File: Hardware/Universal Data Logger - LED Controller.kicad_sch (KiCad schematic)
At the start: 20 parts

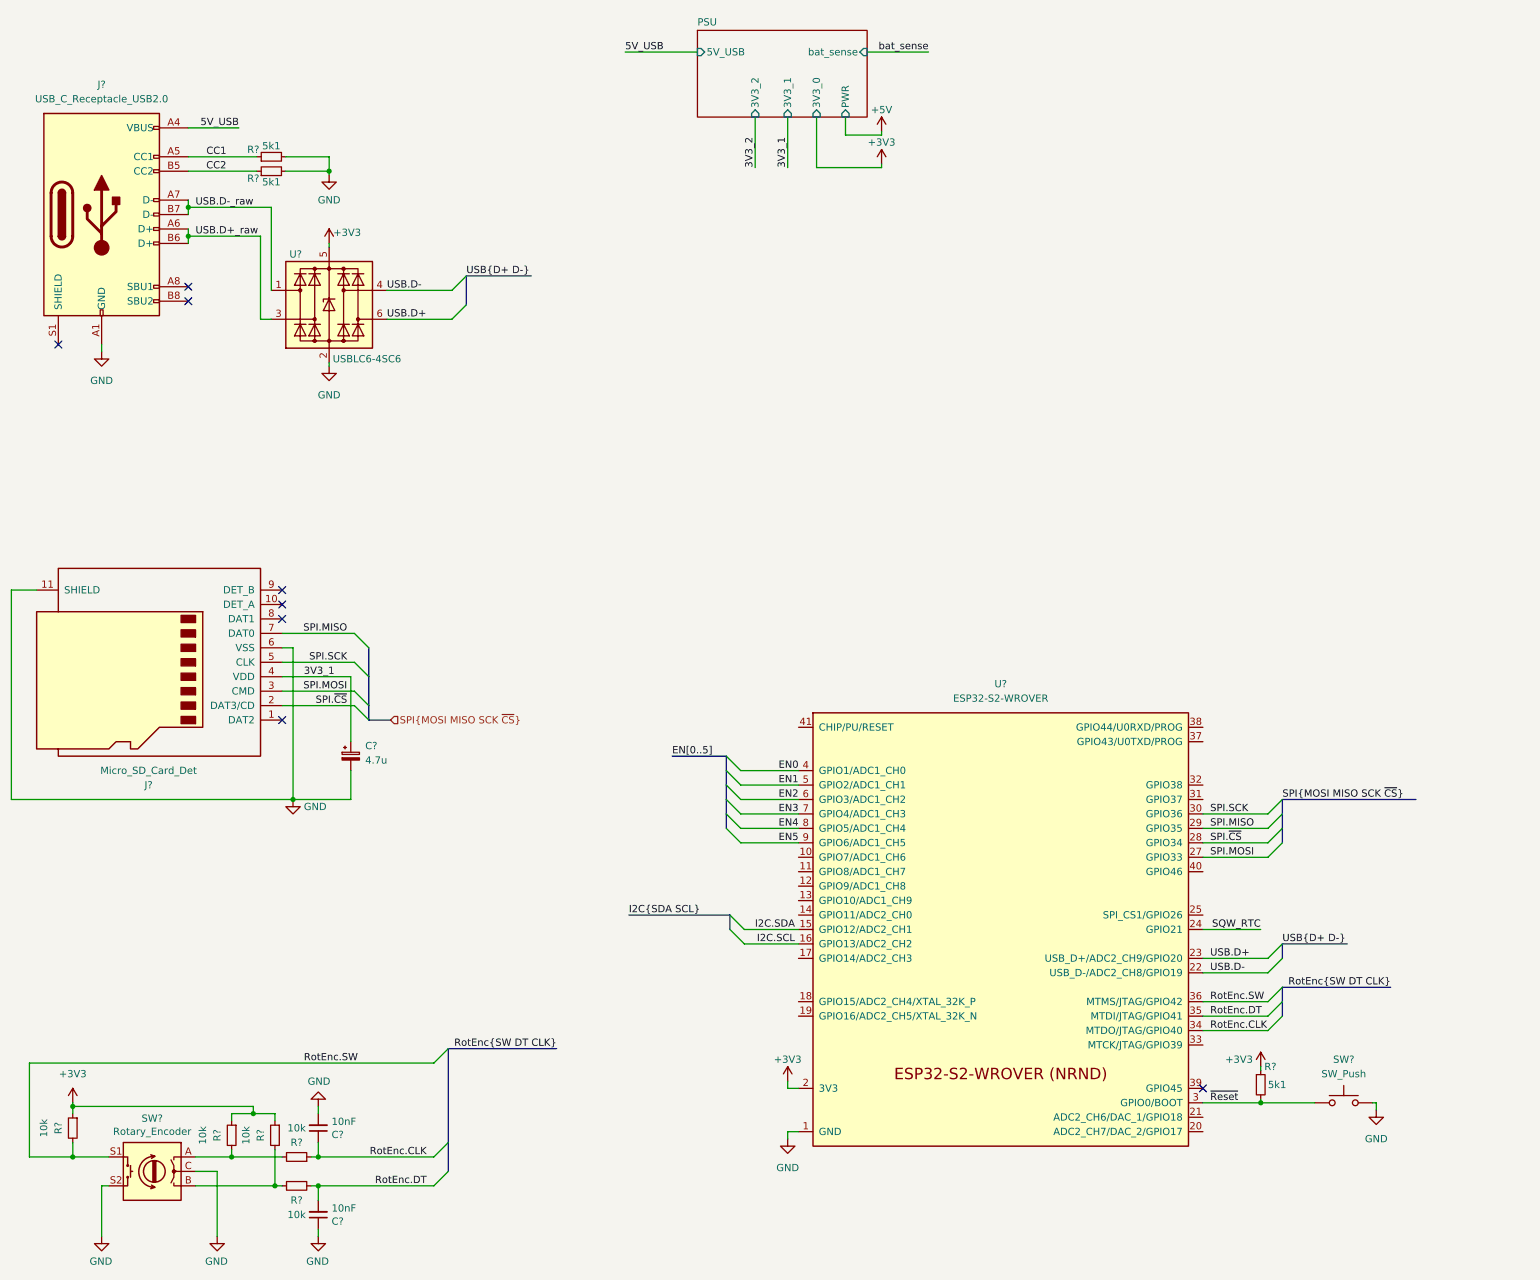
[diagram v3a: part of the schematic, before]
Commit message: added buttons and stuff
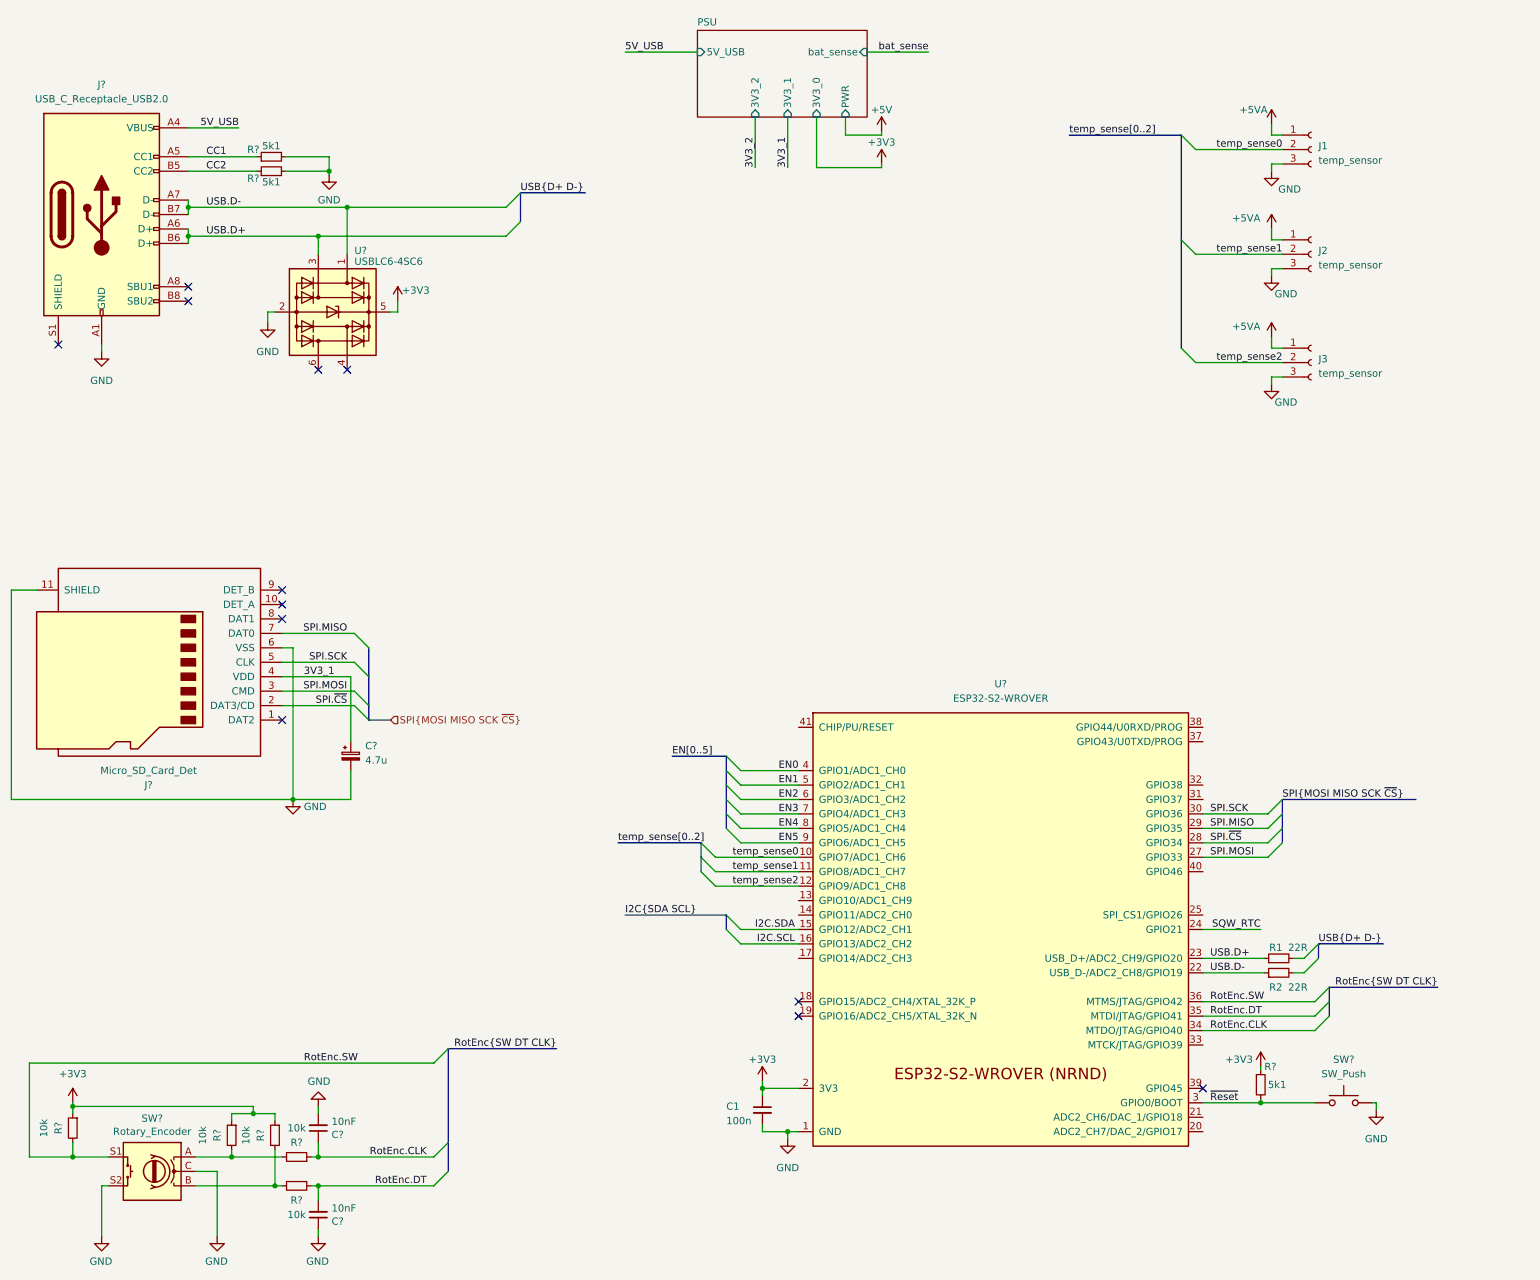
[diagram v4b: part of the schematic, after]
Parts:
- added C1: 100n, symbol Device:C_Small
- added J1, J2, J3: temp_sensor, symbol Connector:Conn_01x03_Socket
- added R1, R2: 22R, symbol Device:R_Small
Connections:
- net USB.D+_raw is gone; now on net USB.D+: J?.A6 (D+), J?.B6 (D+), U?.3 (I/O2)
- net USB.D-_raw is gone; now on net USB.D-: J?.A7 (D-), J?.B7 (D-), U?.1 (I/O1)
- net +3V3: now also C1.1
- net GND: now also C1.2, J1.3 (Pin_3), J2.3 (Pin_3), J3.3 (Pin_3)
- net USB.D+: now also R1.1; no longer U?.6 (I/O4)
- net USB.D-: now also R2.1; no longer U?.4 (I/O3)
- net temp_sense0: now reaches U?.10 (GPIO7/ADC1_CH6)
- net temp_sense0: now also J1.2 (Pin_2)
- net temp_sense1: now reaches U?.11 (GPIO8/ADC1_CH7)
- net temp_sense1: now also J2.2 (Pin_2)
- net temp_sense2: now reaches U?.12 (GPIO9/ADC1_CH8)
- net temp_sense2: now also J3.2 (Pin_2)
- new net +5VA: J1.1 (Pin_1), J2.1 (Pin_1), J3.1 (Pin_1)
- no-connect marks 8 -> 12
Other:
- moved on the sheet: U?
